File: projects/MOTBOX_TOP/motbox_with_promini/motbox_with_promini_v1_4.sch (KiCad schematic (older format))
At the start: 29 parts, among them J1 JST_XH_2pin, J2 Header_3pin_Male, J3 JST_XH_2pin, J4 JST_XH_4pin, J5 JST_XH_2pin, J6 JST_XH_3pin, J7 JST_XH_2pin, P1 Female_Header_12pin, P2 Female_Header_6pin, P3 Female_Header_12pin, U1 LM2576R-5.0, U2 LM393, U3 L293D

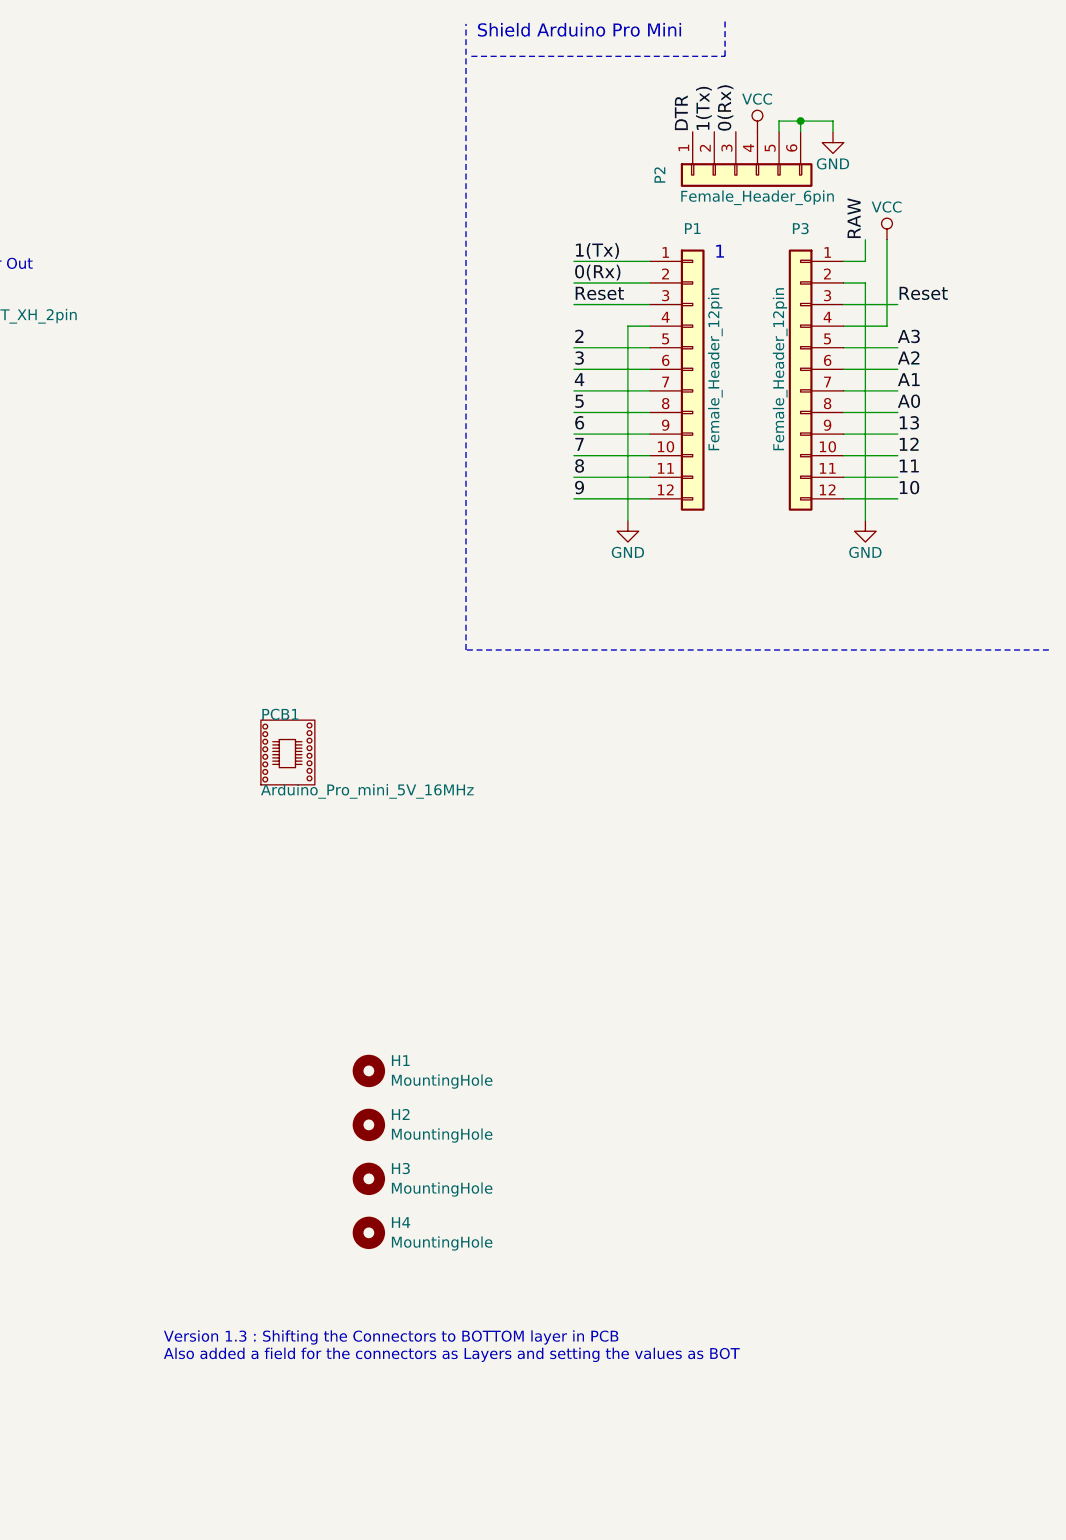
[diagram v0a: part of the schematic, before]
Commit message: Version 1.4 for layout changes related to 12V gnd
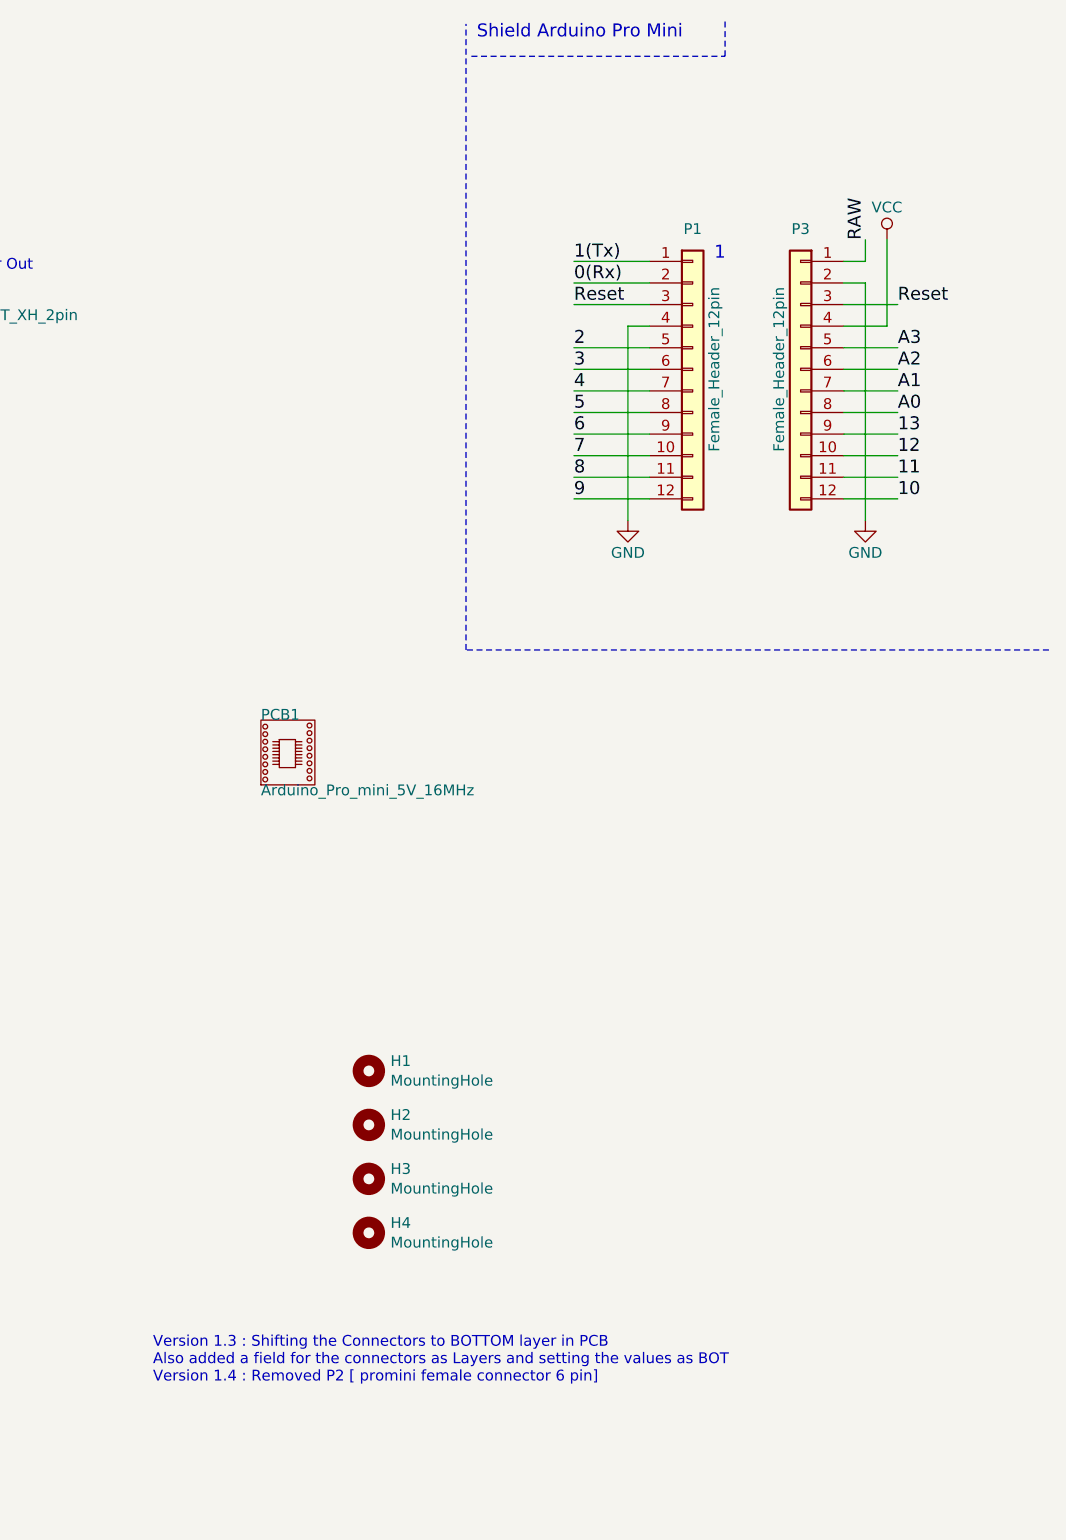
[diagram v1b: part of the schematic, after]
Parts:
- removed P2: Female_Header_6pin, Socket_Arduino_Pro_Mini:Socket_Strip_Arduino_1x06, symbol Connector_Generic:Conn_01x06
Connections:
- net labels removed: DTR
- wire segments 130 -> 125
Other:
- note added: "Version 1.3 : Shifting the Connectors to BOTTOM layer in PCB \nAlso added a field for the connectors as Layers and setting the values as BOT\nVersion 1.4 : Removed P2 [ promini female connector 6 pin]"
- note removed: "Version 1.3 : Shifting the Connectors to BOTTOM layer in PCB \nAlso added a field for the connectors as Layers and setting the values as BOT"
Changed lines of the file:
@@
 Wire Wire Line
 	5000 1300 5000 1400
-Text Notes 7100 6750 0    50   ~ 0
-Version 1.3 : Shifting the Connectors to BOTTOM layer in PCB \nAlso added a field for the connectors as Layers and setting the values as BOT
+Text Notes 7050 6850 0    50   ~ 0
+Version 1.3 : Shifting the Connectors to BOTTOM layer in PCB \nAlso added a field for the connectors as Layers and setting the values as BOT\nVersion 1.4 : Removed P2 [ promini female connector 6 pin]
 $Comp
 L Regulator_Switching_hitesh:LM2576 U1
@@
 	1    0    0    -1
 $EndComp
-$Comp
-L Connector_Generic:Conn_01x06 P2
-U 1 1 56D75238
-P 9750 1250
-F 0 "P2" H 9750 1600 50  0000 C CNN
-F 1 "Female_Header_6pin" V 9850 1150 50  0000 C CNN
-F 2 "Socket_Arduino_Pro_Mini:Socket_Strip_Arduino_1x06" H 9750 1250 50  0001 C CNN
-F 3 "" H 9750 1250 50  0000 C CNN
-F 4 "TOP" H 0   0   50  0001 C CNN "Layer"
-	1    9750 1250
-	0    -1   1    0
-$EndComp
-Text Label 9550 1050 1    60   ~ 0
-DTR
-Text Label 9750 1050 1    60   ~ 0
-0(Rx)
-Text Label 9650 1050 1    60   ~ 0
-1(Tx)
-$Comp
-L power:GND #PWR019
-U 1 1 56D7539A
-P 10200 1050
-F 0 "#PWR019" H 10200 800 50  0001 C CNN
-F 1 "GND" H 10200 900 50  0000 C CNN
-F 2 "" H 10200 1050 50  0000 C CNN
-F 3 "" H 10200 1050 50  0000 C CNN
-	1    10200 1050
-	1    0    0    -1
-$EndComp
-$Comp
-L power:VCC #PWR018
-U 1 1 56D753B8
-P 9850 1050
-F 0 "#PWR018" H 9850 900 50  0001 C CNN
-F 1 "VCC" H 9850 1200 50  0000 C CNN
-F 2 "" H 9850 1050 50  0000 C CNN
-F 3 "" H 9850 1050 50  0000 C CNN
-	1    9850 1050
-	1    0    0    -1
-$EndComp
-Wire Wire Line
-	9950 1050 9950 1000
-Wire Wire Line
-	9950 1000 10050 1000
-Wire Wire Line
-	10050 1000 10050 1050
-Connection ~ 10050 1000
-Wire Wire Line
-	10050 1000 10200 1000
-Wire Wire Line
-	10200 1000 10200 1050
 $EndSCHEMATC

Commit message: Version 1.4
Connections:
- wire segments 125 -> 126
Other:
- note added: "Version 1.3 : Shifting the Connectors to BOTTOM layer in PCB \nAlso added a field for the connectors as Layers and setting the values as BOT\nVersion 1.4 : Removed P2 [ promini female connector 6 pin] \n Connected the IR RX voltage to the A0 pin for \n the transparent ethenet cable detect fix"
- note removed: "Version 1.3 : Shifting the Connectors to BOTTOM layer in PCB \nAlso added a field for the connectors as Layers and setting the values as BOT\nVersion 1.4 : Removed P2 [ promini female connector 6 pin]"
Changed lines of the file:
@@
 EESchema Schematic File Version 4
-LIBS:motbox_with_promini_v1_3-cache
+LIBS:motbox_with_promini_v1_4-cache
 EELAYER 26 0
 EELAYER END
@@
 Wire Wire Line
 	5000 1300 5000 1400
-Text Notes 7050 6850 0    50   ~ 0
-Version 1.3 : Shifting the Connectors to BOTTOM layer in PCB \nAlso added a field for the connectors as Layers and setting the values as BOT\nVersion 1.4 : Removed P2 [ promini female connector 6 pin]
+Text Notes 7250 7000 0    50   ~ 0
+Version 1.3 : Shifting the Connectors to BOTTOM layer in PCB \nAlso added a field for the connectors as Layers and setting the values as BOT\nVersion 1.4 : Removed P2 [ promini female connector 6 pin] \n                            Connected the IR  RX voltage to the A0 pin for \n                            the transparent ethenet cable detect fix
 $Comp
 L Regulator_Switching_hitesh:LM2576 U1
@@
 	1    0    0    -1
 $EndComp
+Wire Wire Line
+	1700 1400 1250 1400
+Text Label 1250 1400 0    50   ~ 0
+A0
 $EndSCHEMATC
